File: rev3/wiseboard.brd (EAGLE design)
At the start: 100 x 80 mm, 58 parts, among them IC1 LT1945, IC2 LM358, IC3 L79L15, IC4 L78L15, IC5 W25Q, IC6 AP2112, IC7 ESP-WROOM-03, IC9 BQ24210DQCT, J1 BAT_CON, J2 SOL_CON, J3 PROG_HEADER, J4 BUT_CON, Q2 IRLML6402TRPBF, SW1 SPST_TACT-KMR2, SW2 SPST_TACT-KMR2

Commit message: Add test points make to do messages
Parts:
- added TP2, TP3, TP4, TP5, TP6: TPSTP20R, testpad:TP20R
- added TP7: TPSTP20SQ, testpad:TP20SQ
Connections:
- net +5V: now also TP6.TP
- net GND: now also TP7.TP
- net GPIO0: now also TP3.TP
- net RESET: now also TP2.TP
- net RXD: now also TP5.TP
- net TXD: now also TP4.TP
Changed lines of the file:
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@@
 <setting verticaltext="up"/>
 </settings>
-<grid distance="50" unitdist="mil" unit="mil" style="lines" multiple="1" display="no" altdistance="5" altunitdist="mil" altunit="mil"/>
+<grid distance="1.27" unitdist="mm" unit="inch" style="lines" multiple="1" display="yes" altdistance="5" altunitdist="mil" altunit="mil"/>
 <layers>
 <layer number="1" name="Top" color="4" fill="1" visible="yes" active="yes"/>
@@
 <element name="L2" library="WISE" package="NR6028T220M" value="NR6028T220M" x="-87.63" y="-1.27"/>
 <element name="IC6" library="WISE" package="SOT95P280X145-5N" value="AP2112" x="-93.98" y="-12.7"/>
+<element name="TP2" library="testpad" library_urn="urn:adsk.eagle:library:385" package="TP20R" value="TPSTP20R" x="-92.71" y="-19.05">
+<attribute name="TP_SIGNAL_NAME" value="" x="-92.71" y="-19.05" size="1.778" layer="27" display="off"/>
+</element>
+<element name="TP3" library="testpad" library_urn="urn:adsk.eagle:library:385" package="TP20R" value="TPSTP20R" x="-92.71" y="-24.13">
+<attribute name="TP_SIGNAL_NAME" value="" x="-92.71" y="-24.13" size="1.778" layer="27" display="off"/>
+</element>
+<element name="TP4" library="testpad" library_urn="urn:adsk.eagle:library:385" package="TP20R" value="TPSTP20R" x="-92.71" y="-29.21">
+<attribute name="TP_SIGNAL_NAME" value="" x="-92.71" y="-29.21" size="1.778" layer="27" display="off"/>
+</element>
+<element name="TP5" library="testpad" library_urn="urn:adsk.eagle:library:385" package="TP20R" value="TPSTP20R" x="-92.71" y="-34.29">
+<attribute name="TP_SIGNAL_NAME" value="" x="-92.71" y="-34.29" size="1.778" layer="27" display="off"/>
+</element>
+<element name="TP6" library="testpad" library_urn="urn:adsk.eagle:library:385" package="TP20R" value="TPSTP20R" x="-92.71" y="-39.37">
+<attribute name="TP_SIGNAL_NAME" value="" x="-92.71" y="-39.37" size="1.778" layer="27" display="off"/>
+</element>
+<element name="TP7" library="testpad" library_urn="urn:adsk.eagle:library:385" package="TP20SQ" value="TPSTP20SQ" x="-92.71" y="-44.45">
+<attribute name="TP_SIGNAL_NAME" value="" x="-92.71" y="-44.45" size="1.778" layer="27" display="off"/>
+</element>
 </elements>
 <signals>
@@
 <contactref element="IC9" pad="9"/>
 <contactref element="IC9" pad="11"/>
+<contactref element="TP7" pad="TP"/>
+<wire x1="-95.28" y1="-12.7" x2="-92.71" y2="-44.45" width="0" layer="19" extent="1-1"/>
 <wire x1="-64.4144" y1="6.35" x2="-95.28" y2="-12.7" width="0" layer="19" extent="1-1"/>
 <wire x1="-60.0456" y1="5.842" x2="-64.4144" y2="6.35" width="0" layer="19" extent="1-1"/>
@@
 <contactref element="J3" pad="1"/>
 <contactref element="IC7" pad="35"/>
-<wire x1="-25.32" y1="1.16" x2="-34.29" y2="59.944" width="0" layer="19" extent="1-1"/>
+<contactref element="TP4" pad="TP"/>
+<wire x1="-25.32" y1="1.16" x2="-92.71" y2="-29.21" width="0" layer="19" extent="1-1"/>
+<wire x1="-34.29" y1="59.944" x2="-25.32" y2="1.16" width="0" layer="19" extent="1-1"/>
 </signal>
 <signal name="GPIO0">
@@
 <contactref element="SW1" pad="4"/>
 <contactref element="IC7" pad="25"/>
+<contactref element="TP3" pad="TP"/>
+<wire x1="-38.02" y1="1.16" x2="-92.71" y2="-24.13" width="0" layer="19" extent="1-1"/>
 <wire x1="-49.21" y1="46.99" x2="-38.02" y2="1.16" width="0" layer="19" extent="1-1"/>
 <wire x1="-62.77" y1="63.97" x2="-49.21" y2="46.99" width="0" layer="19" extent="1-1"/>
@@
 <contactref element="SW2" pad="4"/>
 <contactref element="IC7" pad="3"/>
-<wire x1="-18.51" y1="69.05" x2="-14.51" y2="69.05" width="0" layer="19" extent="1-1"/>
-<wire x1="-36.51" y1="46.99" x2="-18.51" y2="69.05" width="0" layer="19" extent="1-1"/>
-<wire x1="-24.05" y1="19.16" x2="-36.51" y2="46.99" width="0" layer="19" extent="1-1"/>
+<contactref element="TP2" pad="TP"/>
+<wire x1="-24.05" y1="19.16" x2="-92.71" y2="-19.05" width="0" layer="19" extent="1-1"/>
+<wire x1="-36.51" y1="46.99" x2="-24.05" y2="19.16" width="0" layer="19" extent="1-1"/>
+<wire x1="-18.51" y1="69.05" x2="-36.51" y2="46.99" width="0" layer="19" extent="1-1"/>
+<wire x1="-14.51" y1="69.05" x2="-18.51" y2="69.05" width="0" layer="19" extent="1-1"/>
 </signal>
 <signal name="+3V3">
@@
 <contactref element="D3" pad="A"/>
 <contactref element="IC7" pad="34"/>
+<contactref element="TP5" pad="TP"/>
+<wire x1="-26.59" y1="1.16" x2="-92.71" y2="-34.29" width="0" layer="19" extent="1-1"/>
 <wire x1="-56.57" y1="64.77" x2="-26.59" y2="1.16" width="0" layer="19" extent="1-1"/>
 </signal>
@@
 <contactref element="D2" pad="C"/>
 <contactref element="IC6" pad="1"/>
+<contactref element="TP6" pad="TP"/>
+<wire x1="-95.28" y1="-11.75" x2="-92.71" y2="-39.37" width="0" layer="19" extent="1-1"/>
 <wire x1="-42.86" y1="46.99" x2="-95.28" y2="-11.75" width="0" layer="19" extent="1-1"/>
 <wire x1="-41.91" y1="59.944" x2="-42.86" y2="46.99" width="0" layer="19" extent="1-1"/>

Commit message: Start new pcb
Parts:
- removed D6: SS24, WISE:DO214AA
- removed TP2, TP3, TP4, TP5, TP6: TPSTP20R, testpad:TP20R
- removed TP7: TPSTP20SQ, testpad:TP20SQ
- added 3V3, 5V, IO0, RST, RXD, TXD: TPSTP20R, testpad:TP20R
- added GND: TPSTP20SQ, testpad:TP20SQ
- C3: value 1uF -> 0.1uF
- D1: value MBR120VLSFT1G -> MBR120; device microbuilder:SOD-123 -> adafruit:SOD-123
- D2: value MBR120 -> 1n4148
- D3: value 1n4148 -> SS24; device adafruit:SOD-123 -> WISE:DO214AA
- moved L2 136.9 mm to (49.0, 7.00)
- moved SW1 133.4 mm to (56.0, 8.00), turned to 90 degrees
- moved IC6 125.9 mm to (26.0, 25.5), turned to 90 degrees
- moved D3 116.8 mm to (49.0, 19.0)
- moved L1 115.0 mm to (41.0, 7.00)
- moved D2 107.2 mm to (49.5, 30.5)
- moved R1 105.9 mm to (32.0, 7.00), turned to 90 degrees
- moved C3 103.3 mm to (43.0, 13.0)
- moved R3 102.7 mm to (43.0, 17.0)
- moved IC1 101.6 mm to (39.0, 15.0), turned to 270 degrees
- moved Q2 101.3 mm to (34.0, 11.0), turned to 270 degrees
- moved R6 97.5 mm to (31.0, 14.5), turned to 180 degrees
- moved C6 97.4 mm to (36.5, 26.5), turned to 90 degrees
- moved D5 94.3 mm to (49.0, 13.0), turned to 180 degrees
- moved C1 92.7 mm to (45.5, 22.5), turned to 270 degrees
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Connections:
- removed net N$3: C8.2, D1.C, IC9.1
- removed net VOUT: IC6.5
- net +22V: now also D5.C; no longer D6.C
- net +3V3: now also 3V3.TP, IC6.5
- net +5V: now also 5V.TP, D1.C; no longer D2.C, TP6.TP
- net -20V: now also D3.A; no longer D5.A
- net GND: now also GND.TP; no longer IC4.6, IC4.7, TP7.TP
- net GPIO0: now also IO0.TP; no longer TP3.TP
- net N$5: now also D5.A; no longer D6.A
- net N$6: now also D3.C; no longer D5.C
- net PANEL: now also C8.2, IC9.1; no longer D1.A
- net RESET: now also RST.TP; no longer TP2.TP
- net RXD: now also D2.A, RXD.TP; no longer D3.A, TP5.TP
- net RXD_5V: now also D2.C; no longer D3.C
- net TXD: now also TXD.TP; no longer TP4.TP
- net VBAT: now also D1.A; no longer D2.A
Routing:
- net -15V: track 0.00 -> 56.8 mm, vias 0 -> 2
- net +3V3: track 0.00 -> 54.7 mm, vias 0 -> 6
- net D4: track 0.00 -> 53.6 mm, vias 0 -> 3
- net +15V: track 0.00 -> 45.8 mm, vias 0 -> 5
- net +22V: track 0.00 -> 37.2 mm, vias 0 -> 2
- net -20V: track 0.00 -> 35.9 mm, vias 0 -> 2
- net VCOMMON: track 0.00 -> 35.3 mm, vias 0 -> 2
- net D2: track 0.00 -> 34.2 mm, vias 0 -> 2
- net LE: track 0.00 -> 28.4 mm
- net SPH: track 0.00 -> 25.8 mm, vias 0 -> 2
- net GND: track 0.00 -> 24.9 mm, vias 0 -> 5
- net OE: track 0.00 -> 19.9 mm
- net D5: track 0.00 -> 18.8 mm, vias 0 -> 2
- net CL: track 0.00 -> 17.6 mm, vias 0 -> 2
- net D3: track 0.00 -> 15.9 mm, vias 0 -> 2
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- added copper zone on layer 1, net GND
- added copper zone on layer 16, net GND
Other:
- board size 100 x 80 mm -> 60 x 34.5 mm
- board text added: "5V"
- board text added: "GND"
- board text added: "RXD"
- board text added: "TXD"

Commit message: finish layout of PCB
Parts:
- added +15V, +22V, -15V, -20V: TPSTP20R, testpad:TP20R
- added GND17: TPSTP20SQ, testpad:TP20SQ
- moved 3V3 4.46 mm to (27.9, 33.0)
- moved J3 4.16 mm to (46.5, 32.6)
- moved D2 2.18 mm to (51.5, 31.4), turned to 270 degrees
- moved J1 2.16 mm to (18.9, 31.4)
- moved C10 1.58 mm to (18.3, 27.6)
- moved L1 1.41 mm to (40.0, 8.00), turned to 180 degrees
- moved L2 1.41 mm to (48.0, 8.00)
- moved J4 1.06 mm to (37.0, 3.13)
- moved D1 1.00 mm to (21.2, 28.1)
- moved SW2 0.71 mm to (55.5, 14.5)
- moved C8 0.50 mm to (11.0, 29.0)
- moved R36 0.50 mm to (11.0, 27.0)
- moved R37 0.50 mm to (11.0, 25.0)
- moved R38 0.50 mm to (11.0, 23.0)
- moved SW1 0.50 mm to (55.5, 8.00)
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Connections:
- net +15V: now also +15V.TP
- net +22V: now also +22V.TP
- net -15V: now also -15V.TP
- net -20V: now also -20V.TP
- net GND: now also GND17.TP
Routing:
- net GPIO0: track 0.00 -> 142.3 mm, vias 0 -> 6
- net GND: track 24.9 -> 159.6 mm, vias 5 -> 31
- net RESET: track 0.00 -> 102.7 mm, vias 0 -> 4
- net +3V3: track 54.7 -> 150.7 mm, vias 6 -> 8
- net VBAT: track 0.00 -> 88.6 mm, vias 0 -> 7
- net +22V: track 37.2 -> 120.6 mm, vias 2 -> 7
- net TXD: track 0.00 -> 78.8 mm, vias 0 -> 5
- net RXD: track 0.00 -> 74.6 mm, vias 0 -> 4
- net +5V: track 0.00 -> 56.3 mm, vias 0 -> 2
- net PANEL: track 0.00 -> 55.9 mm, vias 0 -> 3
- net -20V: track 35.9 -> 88.2 mm, vias 2 -> 7
- net N$9: track 0.00 -> 31.8 mm, vias 0 -> 2
- net POSEN: track 0.00 -> 29.9 mm
- net N$8: track 0.00 -> 29.1 mm, vias 0 -> 4
- net -15V: track 56.8 -> 84.3 mm
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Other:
- board size 60 x 34.5 mm -> 58 x 34.5 mm
- board text added: "BAT"
- board text added: "BTN"
- board text added: "Board By:"
- board text added: "SOL"
- board text added: "WISE Mk3"

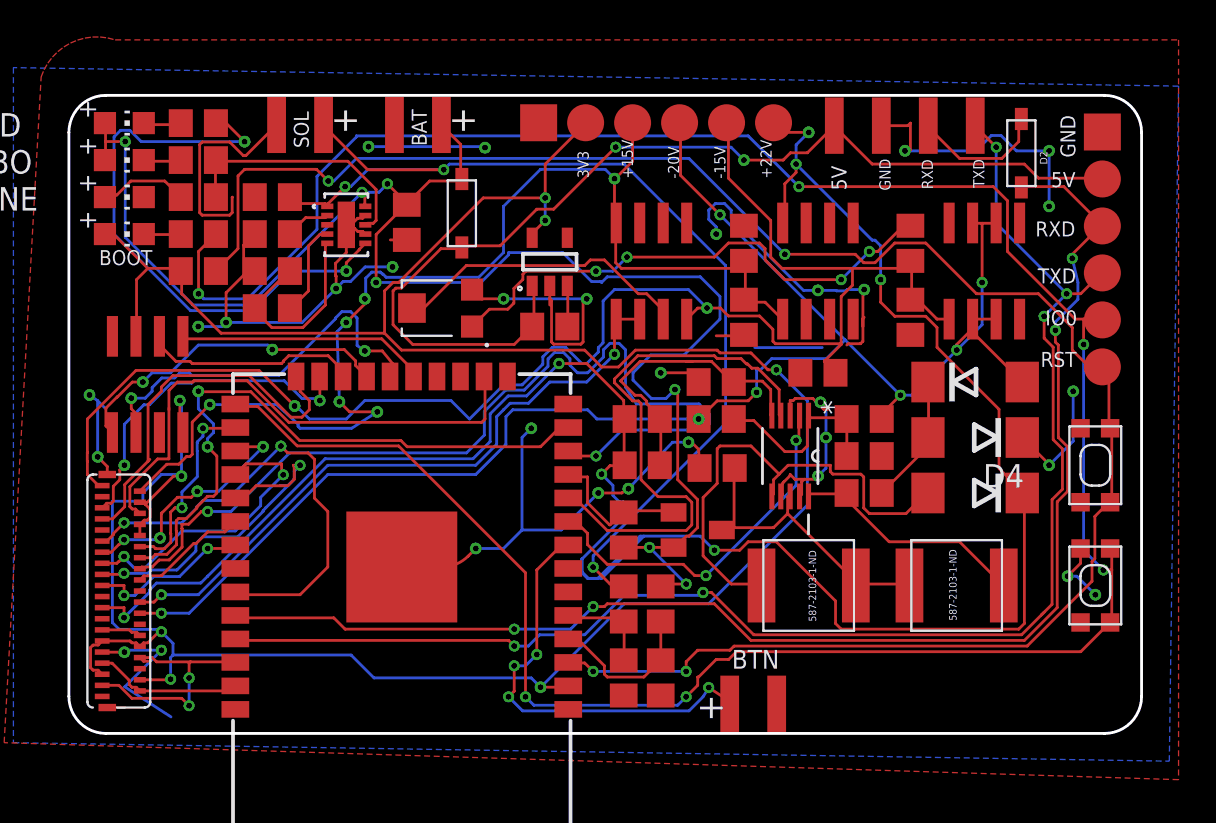
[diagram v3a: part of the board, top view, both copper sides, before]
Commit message: Fix REST GPIO0 Intersection
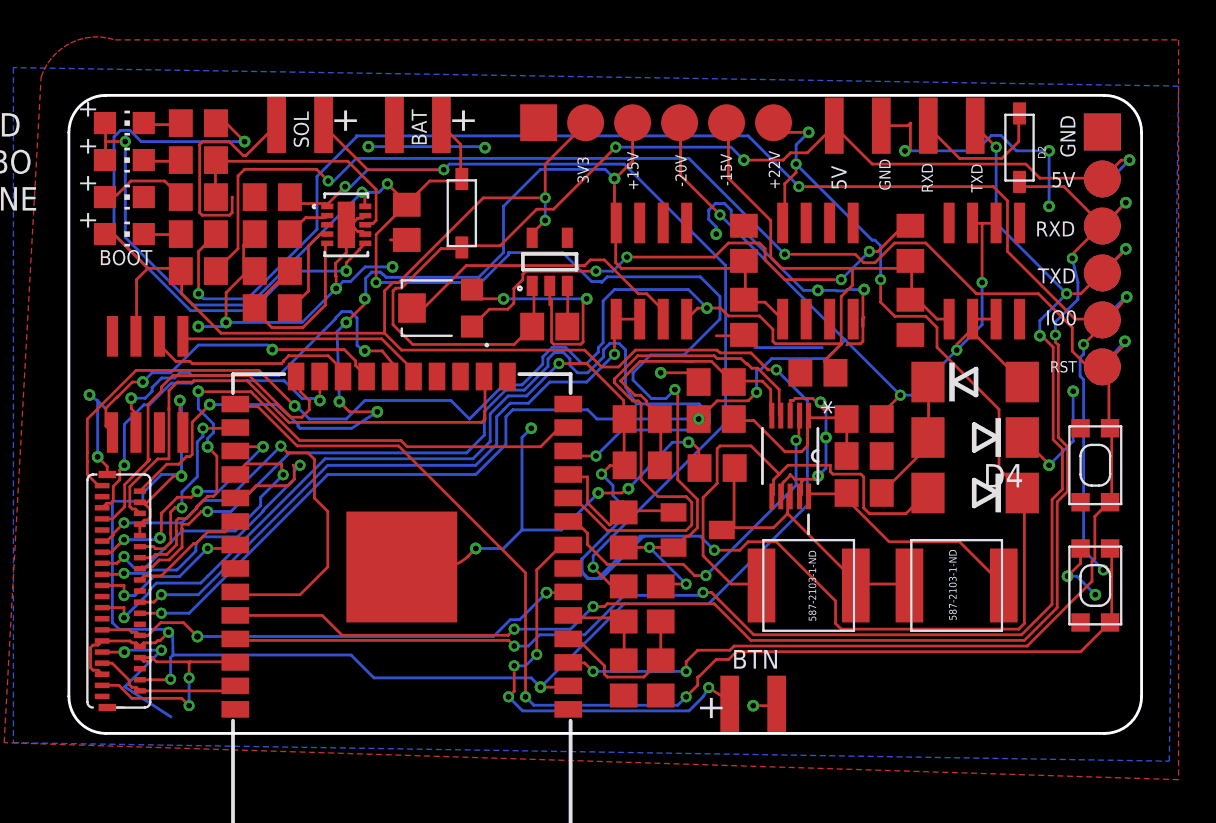
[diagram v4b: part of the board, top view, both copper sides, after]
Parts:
- added 5V1, IO1, RST1, RXD1, TXD1: TPSTP20R, testpad:TP20R
- added GND23: TPSTP20SQ, testpad:TP20SQ
- C1, C6: value 1uF -> 1uF > 15V
- C10, C8: value 10uF -> 1uF
- C2: value 1uF -> 4.7uF
- C3: value 0.1uF -> 1uF
- C4: value 10uF -> 100pF
- C5: value 10uF -> 4.7pF > 22V
- R3: value 470k -> 560k > 20V
- R4: value 39k -> 39k > 20V
- moved D2 0.32 mm to (51.4, 31.7)
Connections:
- removed net N$48: IC7.6
- net +5V: now also 5V1.TP
- net GMODE: now also IC7.6
- net GND: now also GND23.TP
- net GPIO0: now also IO1.TP
- net RESET: now also RST1.TP
- net RXD: now also RXD1.TP
- net TXD: now also TXD1.TP
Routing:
- net GMODE: track 2.16 -> 26.9 mm, vias 0 -> 2
- net GPIO0: track 142.3 -> 147.4 mm, vias 6 -> 7
- net RXD: track 74.6 -> 78.9 mm, vias 4 -> 5
- net RESET: track 102.7 -> 106.5 mm, vias 4 -> 5
- net +5V: track 56.3 -> 60.1 mm, vias 2 -> 3
- net TXD: track 78.8 -> 82.5 mm, vias 5 -> 6
- net GND: track 159.6 -> 160.9 mm, vias 31 -> 32
- net +3V3: track 150.7 -> 151.3 mm
